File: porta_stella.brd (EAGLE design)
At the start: 79 x 89.9 mm, 107 parts, among them CN4 MicroUSB, IC1 74LS00D, J1 2p-smd-1.0-90d, J2 SJ-43516-SMT, SW1 E-SWITCH_JS5208E-SWITCH_JS520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, T1 2N3904, T2 PN3906, T3 PN3906, T4 PN3906, T5 MMUN2133LT1G, U1 TPS61090RSAR, U2 MCP73871, X1 SSW-112-02-G-Q

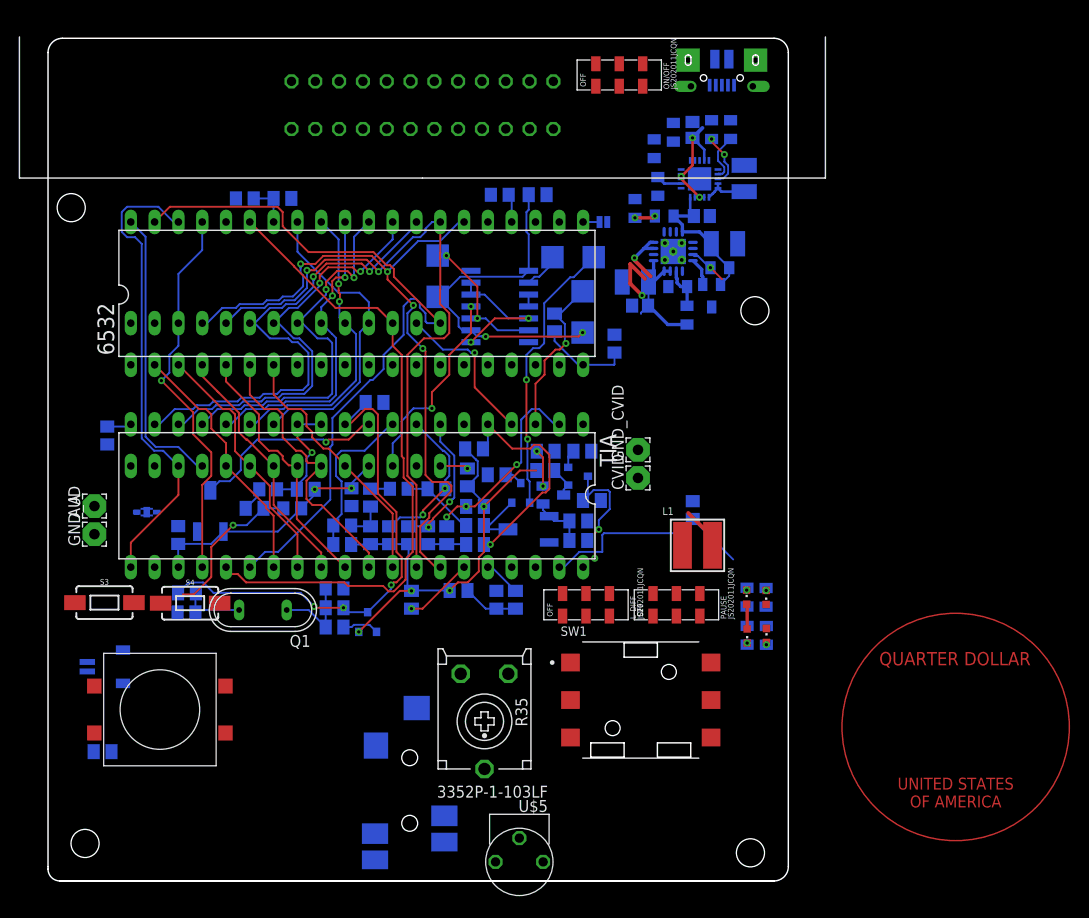
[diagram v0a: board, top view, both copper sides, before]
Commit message: Finished traces, just need to label components:
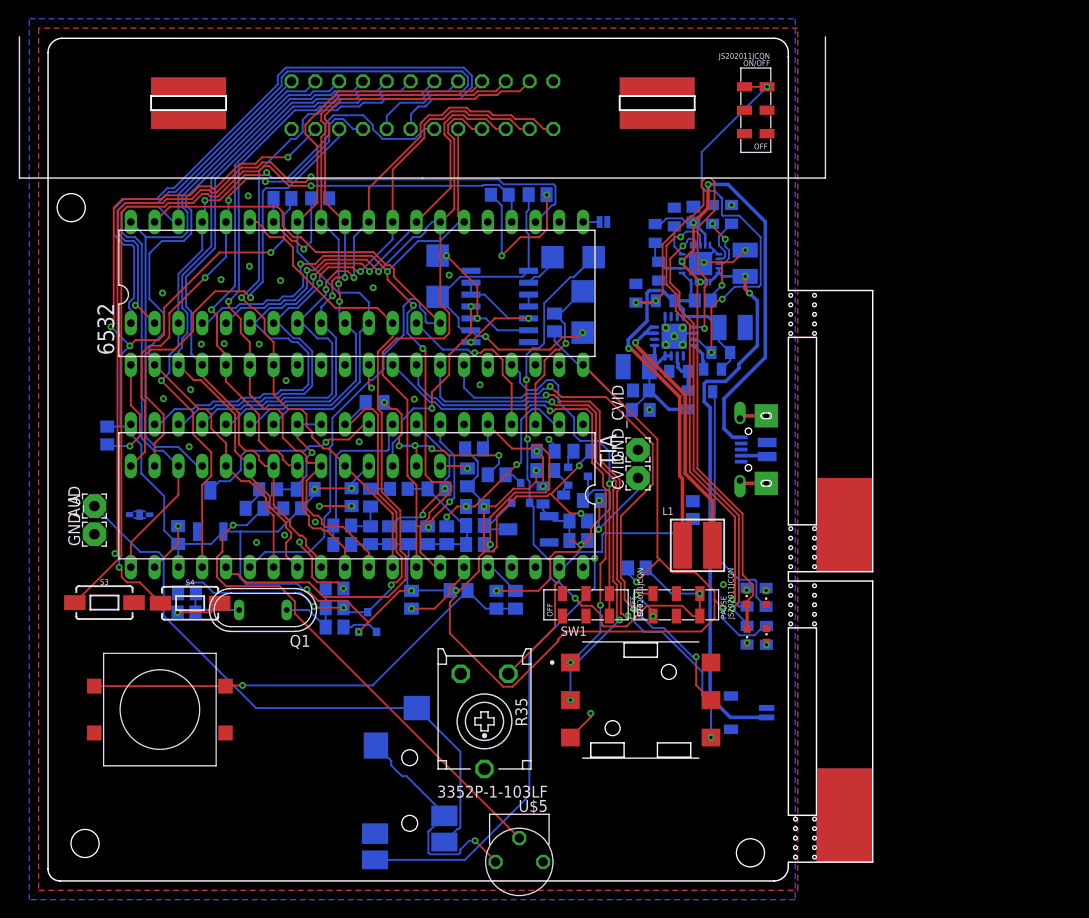
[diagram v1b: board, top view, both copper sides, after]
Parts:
- moved J1 71.9 mm to (76.3, 18.0), turned to 180 degrees
- moved R34 60.3 mm to (62.8, 33.4), turned to 180 degrees
- moved CN4 39.8 mm to (74.7, 46.0), turned to 270 degrees
- moved ON/OFF 15.0 mm to (75.5, 82.2), turned to 90 degrees
- moved C21 9.04 mm to (74.4, 65.9)
- moved C22 9.04 mm to (68.9, 71.1)
- moved C6 9.04 mm to (63.3, 52.3)
- moved C9 9.04 mm to (62.8, 54.9)
- moved R37 9.04 mm to (71.8, 56.4)
- moved R38 9.04 mm to (68.3, 51.3)
- moved R39 9.04 mm to (67.3, 54.4)
- moved R41 9.04 mm to (65.9, 61.9)
- moved R42 9.04 mm to (64.8, 69.1)
- moved R43 9.04 mm to (65.2, 65.1)
- moved R46 9.04 mm to (70.9, 71.1)
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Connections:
- removed net JACK_AUD_OUT_L: J2.5
- removed net JACK_AUD_OUT_R: J2.6
- removed net N$25: CVID.1, R25.1, T2.3
- removed net N$8: AUD.1
- new net JACK_AUD_OUT: AUD.1, J2.5, J2.6
- net CVID: now also CVID.1, R25.1, T2.3
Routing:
- net +5V: track 102.6 -> 330.2 mm, vias 6 -> 16
- net GND: track 0.00 -> 131.6 mm, vias 0 -> 47
- net N$19: track 0.00 -> 100.2 mm, vias 0 -> 3
- net N$18: track 3.03 -> 91.7 mm, vias 0 -> 1
- net VBUS: track 16.3 -> 95.3 mm, vias 3 -> 4
- net A11: track 0.00 -> 71.1 mm, vias 0 -> 1
- net A10: track 0.00 -> 70.0 mm
- net CVID: track 0.00 -> 68.7 mm, vias 0 -> 2
- net JACK_AUD_OUT: track 0.00 -> 64.0 mm
- net LFT_JOY_LFT: track 0.00 -> 63.1 mm, vias 0 -> 3
- net LFT_JOY_RGT: track 0.00 -> 59.7 mm, vias 0 -> 3
- net LFT_JOY_DWN: track 0.00 -> 57.0 mm, vias 0 -> 3
- net VLIPO: track 4.82 -> 61.0 mm, vias 0 -> 2
- net A9: track 0.00 -> 53.6 mm, vias 0 -> 3
- net LFT_JOY_UP: track 0.00 -> 52.6 mm, vias 0 -> 3
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- added copper zone on layer 1, net GND
- added copper zone on layer 16, net GND
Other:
- board size 79 x 89.9 mm -> 88 x 89.9 mm
- board text removed: "QUARTER DOLLAR"
- board text removed: "UNITED STATES OF AMERICA"

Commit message: ready for manufacturing
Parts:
- removed U$5: 3352P-1-103LF, tiny_stella:3352P-1-103LF
- added GOLD_ORB_SM1: OSHWLOGOLOGO5MM, tiny_stella:OSHW_5MM
- added VOL: 3352P-1-103LF, tiny_stella:3352P-1-103LF
- TIA: value ATARI_TIA -> TIA
- moved CHRG/LBO 2.00 mm to (74.5, 28.3)
- moved DONE 2.00 mm to (74.6, 24.1)
- moved LBO 2.00 mm to (76.6, 28.2)
- moved ON 2.00 mm to (76.7, 24.2)
- moved R13 2.00 mm to (76.6, 28.3)
- moved R36 2.00 mm to (76.7, 24.2)
- moved R44 2.00 mm to (74.6, 28.3)
- moved R45 2.00 mm to (74.6, 24.2)
- renumbered BRIGHT to BRT, R35 to LFT_PADDLE
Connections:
- net AUD: now also VOL.P$1; no longer U$5.P$1
- net GND: now also VOL.P$2; no longer U$5.P$2
- net N$28: now also VOL.P$3; no longer U$5.P$3
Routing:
- net AUD: track 24.5 -> 32.4 mm
- net N$28: track 56.9 -> 64.2 mm
- net VBUS: track 95.3 -> 97.3 mm
- net N$45: track 48.2 -> 50.2 mm
- net N$44: track 47.4 -> 49.4 mm
- net +5V: track 330.2 -> 332.2 mm
- net N$41: track 26.3 -> 27.7 mm
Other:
- outline, holes or cut-outs redrawn
- board text added: "AUD+"
- board text added: "AUD-"
- board text added: "Board Rev 1.0"
- board text added: "CHRG"
- board text added: "CHRGD"
- board text added: "Designed 10 Miles from Sunnyvale"
- board text added: "GND"
- board text added: "LOW BAT"
- board text added: "ON"
- board text added: "T5"
- board text added: "TinyTari Portable"

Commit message: worked on the BOM
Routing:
- net LFT_JOY_LFT: track 63.1 -> 61.3 mm
- net D1: track 65.6 -> 64.4 mm
- net LFT_JOY_DWN: track 57.0 -> 56.1 mm
- net A11: track 71.1 -> 71.8 mm
- net A10: track 70.0 -> 70.8 mm
